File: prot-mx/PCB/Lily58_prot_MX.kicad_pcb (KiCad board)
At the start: 2 copper layers, 142.5 x 106.3 mm, 84 parts, among them J1 LED, J2 4PIN, J3 OLED, P1 i2c_pin, P2 i2c_pin, SW1 SW_PUSH, SW10 SW_PUSH, SW11 SW_PUSH, SW12 SW_PUSH, SW13 SW_PUSH, SW14 SW_PUSH, SW15 SW_PUSH, SW16 SW_PUSH, SW17 SW_PUSH, SW18 SW_PUSH, SW19 SW_PUSH, SW2 SW_PUSH, SW20 SW_PUSH, SW21 SW_PUSH, SW22 SW_PUSH, SW23 SW_PUSH, SW24 SW_PUSH, SW25 SW_PUSH, SW26 SW_PUSH, SW27 SW_PUSH, SW28 SW_PUSH, SW29 SW_PUSH, SW3 SW_PUSH, SW30 ROT_ENC_SW, SW4 SW_PUSH, SW5 SW_PUSH, SW6 SW_PUSH, SW7 SW_PUSH, SW8 SW_PUSH, SW9 SW_PUSH, U1 ProMicro

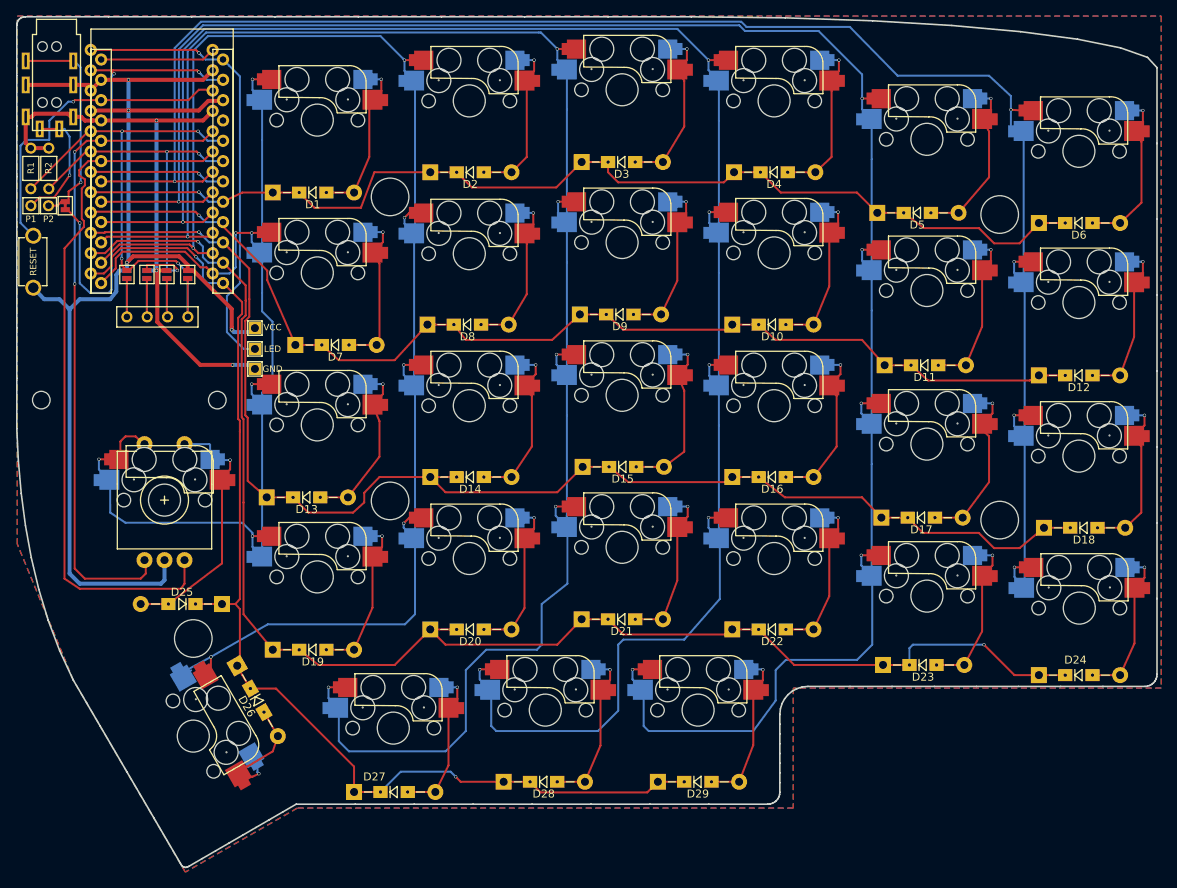
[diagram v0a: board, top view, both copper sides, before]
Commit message: fixed slikscreen labels on PCB (VCC and GND for LEDs swapped to match pad labels) and prettified traces
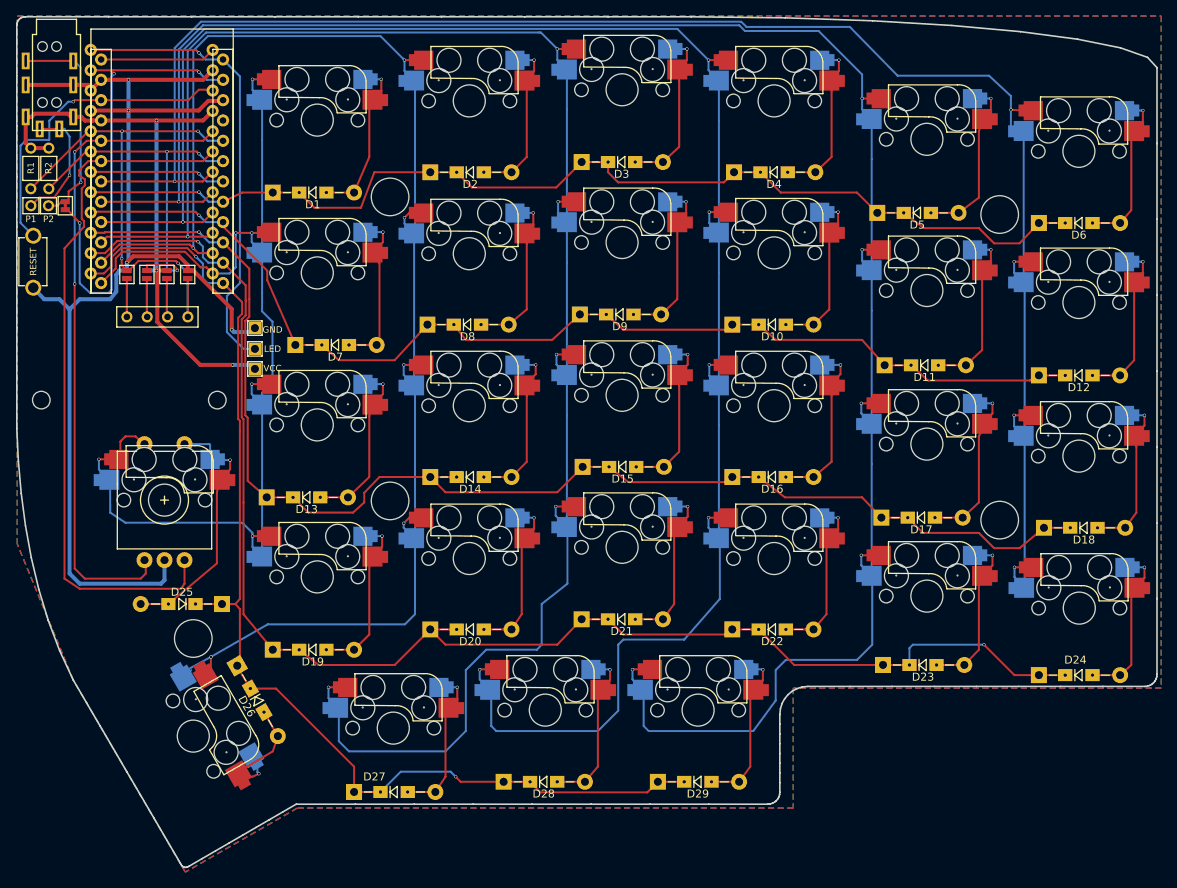
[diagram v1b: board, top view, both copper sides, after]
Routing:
- net Net-(D6-Pad2): track 23.4 -> 22.7 mm
- net Net-(D18-Pad2): track 23.5 -> 22.8 mm
- net Net-(D15-Pad2): track 23.7 -> 23.1 mm
- net R_SW1: track 35.7 -> 35.1 mm
